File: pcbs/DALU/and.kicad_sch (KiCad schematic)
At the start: 3 parts, among them U901 74HC08, U902 74HC08

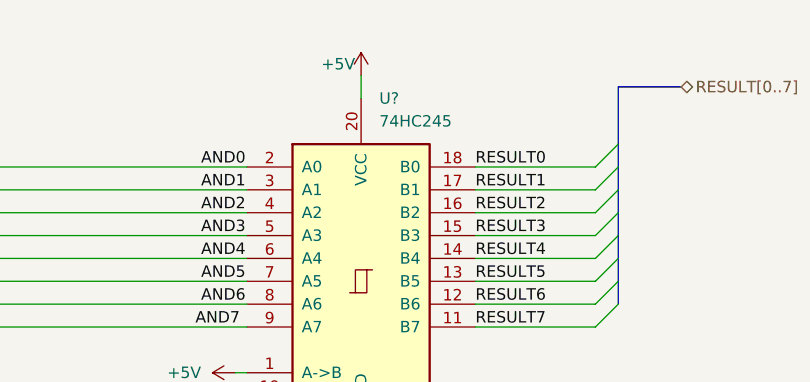
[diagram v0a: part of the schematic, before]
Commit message: Routing.... have realised that I need to think more about vias
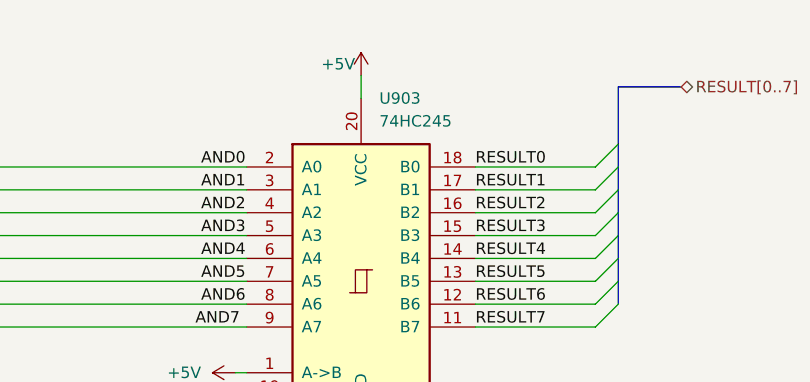
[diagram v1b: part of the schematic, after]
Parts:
- gave numbers to parts that had none: 1
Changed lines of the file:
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@@
+    (stroke (width 0) (type default) (color 0 0 0 0))
+  )
+  (wire (pts (xy 87.63 41.91) (xy 87.63 79.375))
     (stroke (width 0) (type default) (color 0 0 0 0))
   )
@@
   )
   (wire (pts (xy 92.71 109.22) (xy 73.025 109.22))
-    (stroke (width 0) (type default) (color 0 0 0 0))
-  )
-  (wire (pts (xy 87.63 41.91) (xy 87.63 79.375))
     (stroke (width 0) (type default) (color 0 0 0 0))
   )
@@
   (symbol (lib_id "power:+5V") (at 149.86 24.13 0) (unit 1)
     (in_bom yes) (on_board yes)
-    (property "Reference" "#PWR?" (id 0) (at 149.86 27.94 0)
+    (property "Reference" "#PWR0902" (id 0) (at 149.86 27.94 0)
       (effects (font (size 1.27 1.27)) hide)
     )
@@
   (symbol (lib_id "power:+5V") (at 135.89 57.15 90) (unit 1)
     (in_bom yes) (on_board yes) (fields_autoplaced)
-    (property "Reference" "#PWR?" (id 0) (at 139.7 57.15 0)
+    (property "Reference" "#PWR0901" (id 0) (at 139.7 57.15 0)
       (effects (font (size 1.27 1.27)) hide)
     )
@@
   (symbol (lib_id "power:GND") (at 149.86 72.39 0) (unit 1)
     (in_bom yes) (on_board yes) (fields_autoplaced)
-    (property "Reference" "#PWR?" (id 0) (at 149.86 78.74 0)
+    (property "Reference" "#PWR0903" (id 0) (at 149.86 78.74 0)
       (effects (font (size 1.27 1.27)) hide)
     )
@@
   (symbol (lib_id "74xx:74HC245") (at 149.86 46.99 0) (unit 1)
     (in_bom yes) (on_board yes) (fields_autoplaced)
-    (property "Reference" "U?" (id 0) (at 151.8794 26.67 0)
+    (property "Reference" "U903" (id 0) (at 151.8794 26.67 0)
       (effects (font (size 1.27 1.27)) (justify left))
     )

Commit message: Routing, routing, routing
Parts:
- added C901, C902, C903: 100n, Capacitor_SMD:C_0603_1608Metric, symbol Device:C
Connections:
- net +5V: now also U901.14 (VCC), U902.14 (VCC), C901.1, C902.1, C903.1
- net A0: now also U901.9; no longer U901.1
- net A1: now also U901.12; no longer U901.4
- net A2: now also U901.1; no longer U901.9
- net A3: now also U901.4; no longer U901.12
- net AND0: now also U901.8; no longer U901.3
- net AND1: now also U901.11; no longer U901.6
- net AND2: now also U901.3; no longer U901.8
- net AND3: now also U901.6; no longer U901.11
- net B0: now also U901.10; no longer U901.2
- net B1: now also U901.13; no longer U901.5
- net B2: now also U901.2; no longer U901.10
- net B3: now also U901.5; no longer U901.13
- net GND: now also U901.7 (GND), U902.7 (GND), C901.2, C902.2, C903.2
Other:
- moved on the sheet: U901A, U901B, U901C, U901D, U901E, U902E
